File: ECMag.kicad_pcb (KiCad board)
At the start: 2 copper layers, 44 parts, among them J1 Conn_01x12, J2 Conn_01x05, J3 Conn_01x04, J4 USB_B, J5 Barrel_Jack_SW, J6 Conn_01x04, K1 Tactil Switch B3F NA, K2 Tactil Switch B3F NA, K3 Tactil Switch B3F NA, K4 Tactil Switch B3F NA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

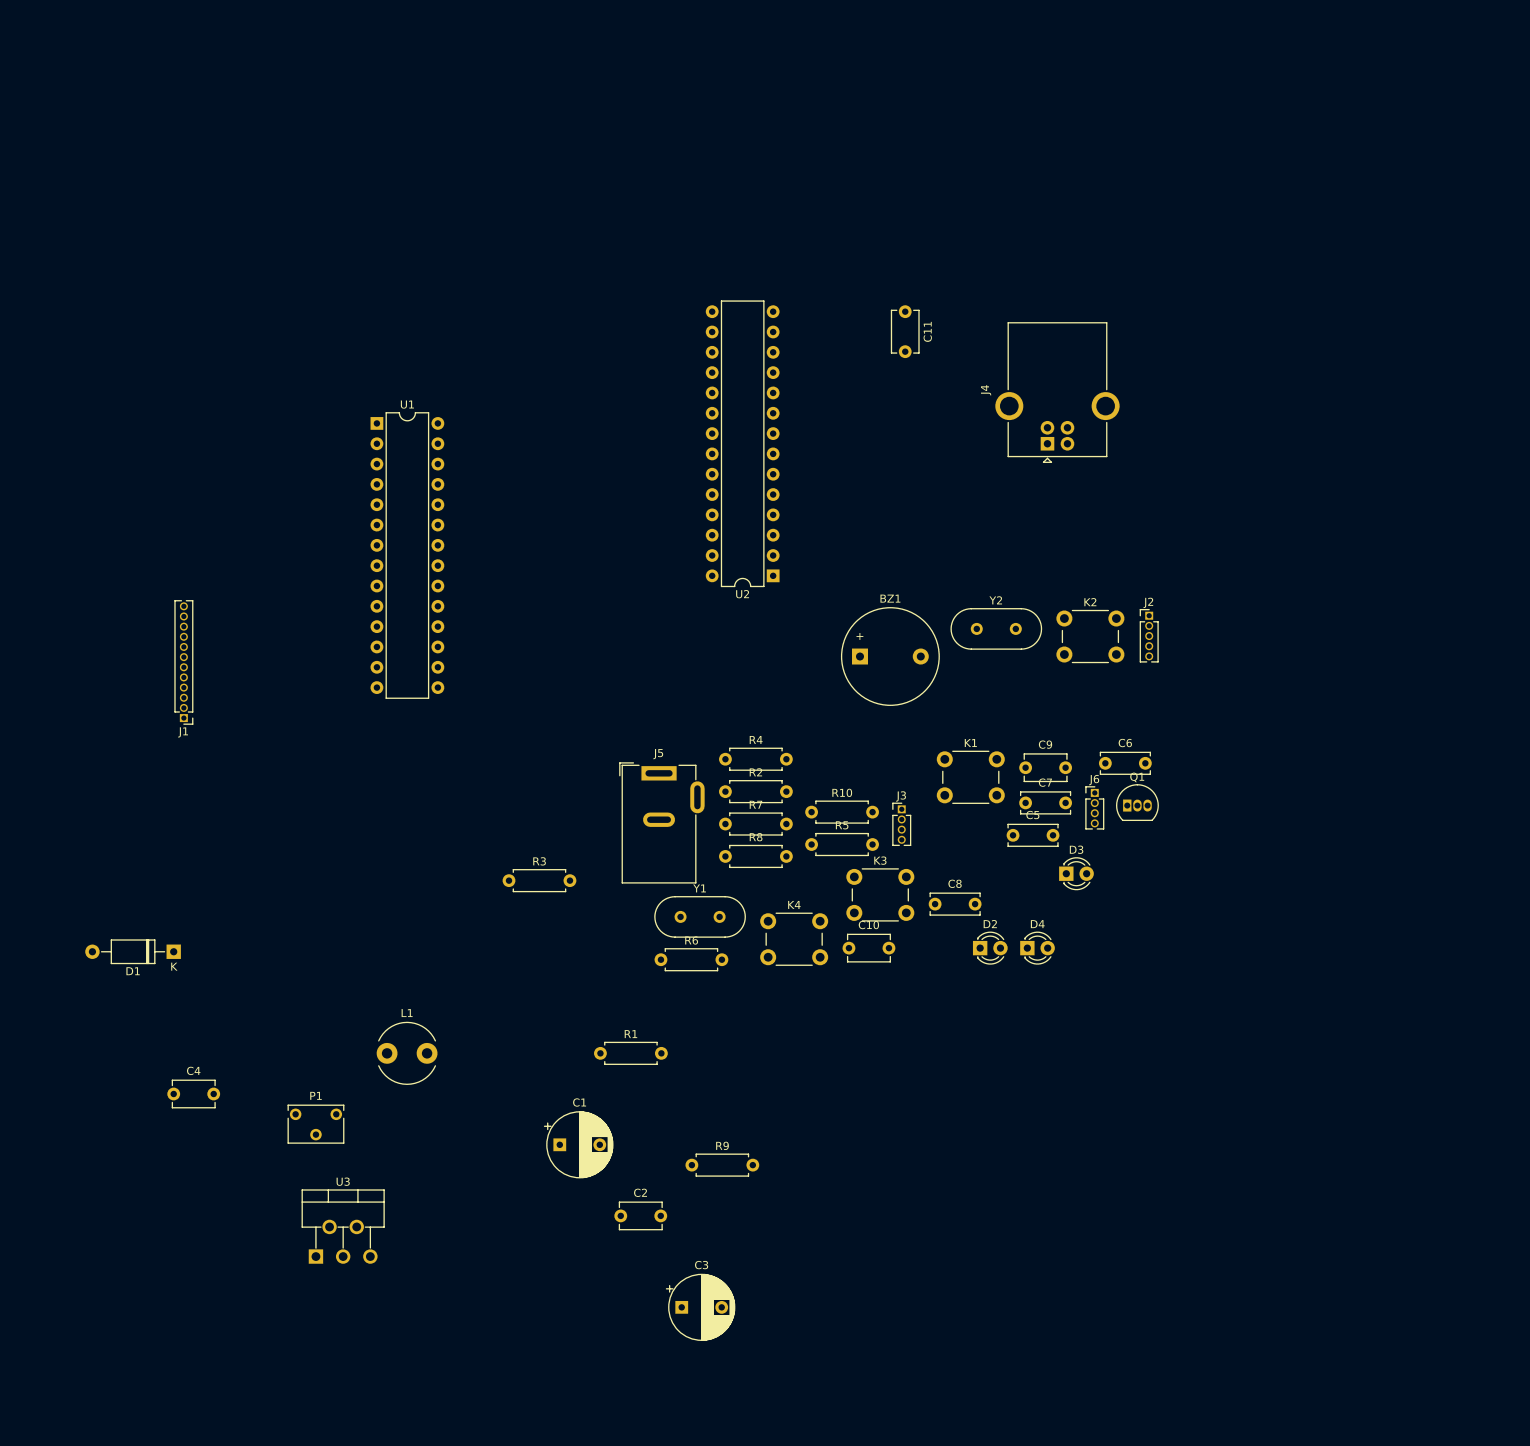
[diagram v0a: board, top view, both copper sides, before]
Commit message: agregado de valores de los componentes en el esquemático
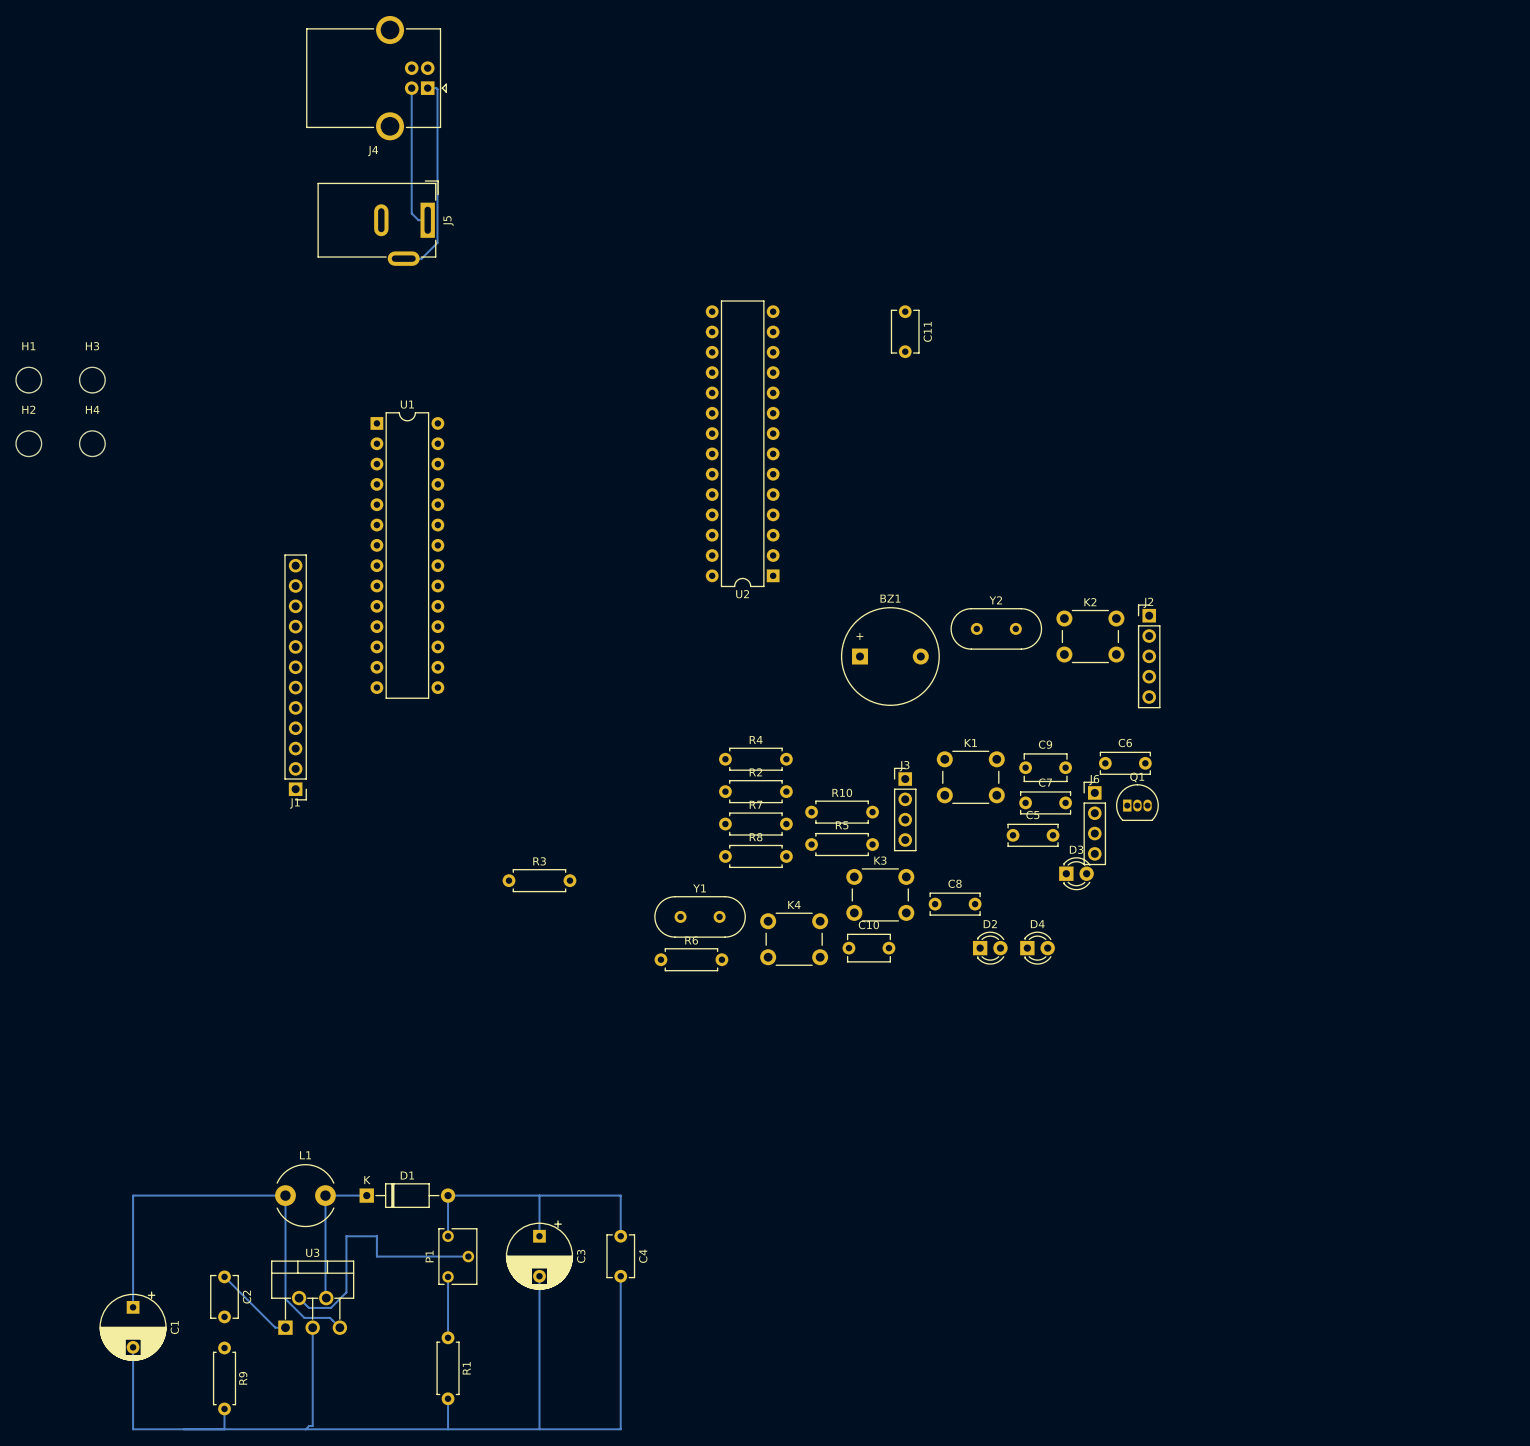
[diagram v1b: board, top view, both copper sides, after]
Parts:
- added H1: MountingHole, MountingHole:MountingHole_3.2mm_M3, F.Cu at (34.0, 61.9)
- added H2: MountingHole, MountingHole:MountingHole_3.2mm_M3, F.Cu at (34.0, 69.8)
- added H3: MountingHole, MountingHole:MountingHole_3.2mm_M3, F.Cu at (41.9, 61.9)
- added H4: MountingHole, MountingHole:MountingHole_3.2mm_M3, F.Cu at (41.9, 69.8)
- BZ1: value Buzzer 5V 85db 2300Hz -> 85db 2300Hz
- C1, C3: value 220uF 25v HT -> 220uF 25v
- C2: value 330nF Cerámico -> 330nF
- C4: value 100nF Cerámico -> 100nF
- D2: value LED Azul -> LED A
- D3: value LED Rojo -> LED R
- D4: value LED Verde -> LED V
- J1: footprint Connector_PinHeader_1.27mm:PinHeader_1x12_P1.27mm_Vertical -> Connector_PinHeader_2.54mm:PinHeader_1x12_P2.54mm_Vertical
- J2: footprint Connector_PinHeader_1.27mm:PinHeader_1x05_P1.27mm_Vertical -> Connector_PinHeader_2.54mm:PinHeader_1x05_P2.54mm_Vertical
- J3, J6: footprint Connector_PinHeader_1.27mm:PinHeader_1x04_P1.27mm_Vertical -> Connector_PinHeader_2.54mm:PinHeader_1x04_P2.54mm_Vertical
- R1: value 2K 1% -> 2K
- R10: value 3K3 5% -> 3K3
- R2, R3, R4, R5: value 10K 5% -> 10K
- R6, R7, R8: value 4K7 5% -> 4K7
- R9: value 2K2 1% -> 2K2
- moved J4 89.3 mm to (83.8, 25.4), turned to 180 degrees
- moved J5 74.9 mm to (83.8, 41.9), turned to 270 degrees
- moved R9 62.7 mm to (58.4, 182.9), turned to 270 degrees
- moved C4 58.6 mm to (108.0, 168.9), turned to 270 degrees
- moved C1 57.1 mm to (47.0, 177.8), turned to 270 degrees
- moved C2 50.1 mm to (58.4, 174.0), turned to 270 degrees
- moved R1 40.3 mm to (86.4, 181.6), turned to 270 degrees
- moved D1 38.9 mm to (76.2, 163.8), turned to 0 degrees
- moved L1 21.8 mm to (66.0, 163.8)
- moved P1 20.7 mm to (86.4, 168.9), turned to 90 degrees
- moved C3 19.9 mm to (97.8, 168.9), turned to 270 degrees
- moved J1 16.6 mm to (67.3, 113.0)
- moved U3 9.67 mm to (66.0, 180.3)
- moved J3 3.81 mm to (143.5, 111.8)
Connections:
- Y1 pad 1: Net-(C5-Pad1) -> Net-(C6-Pad1)
- Y1 pad 2: Net-(C6-Pad1) -> Net-(C5-Pad1)
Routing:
- net GND: track 0.00 -> 152.2 mm
- net +5V: track 0.00 -> 54.2 mm
- net +12V: track 0.00 -> 36.8 mm
- net Net-(P1-Pad2): track 0.00 -> 32.0 mm
- net Net-(J4-Pad1): track 0.00 -> 25.5 mm
- net Net-(D1-Pad1): track 0.00 -> 18.0 mm
- net Net-(C2-Pad1): track 0.00 -> 10.3 mm
- net Net-(P1-Pad3): track 0.00 -> 7.62 mm

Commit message: Edicion de huella de pulsadores y primer pcb
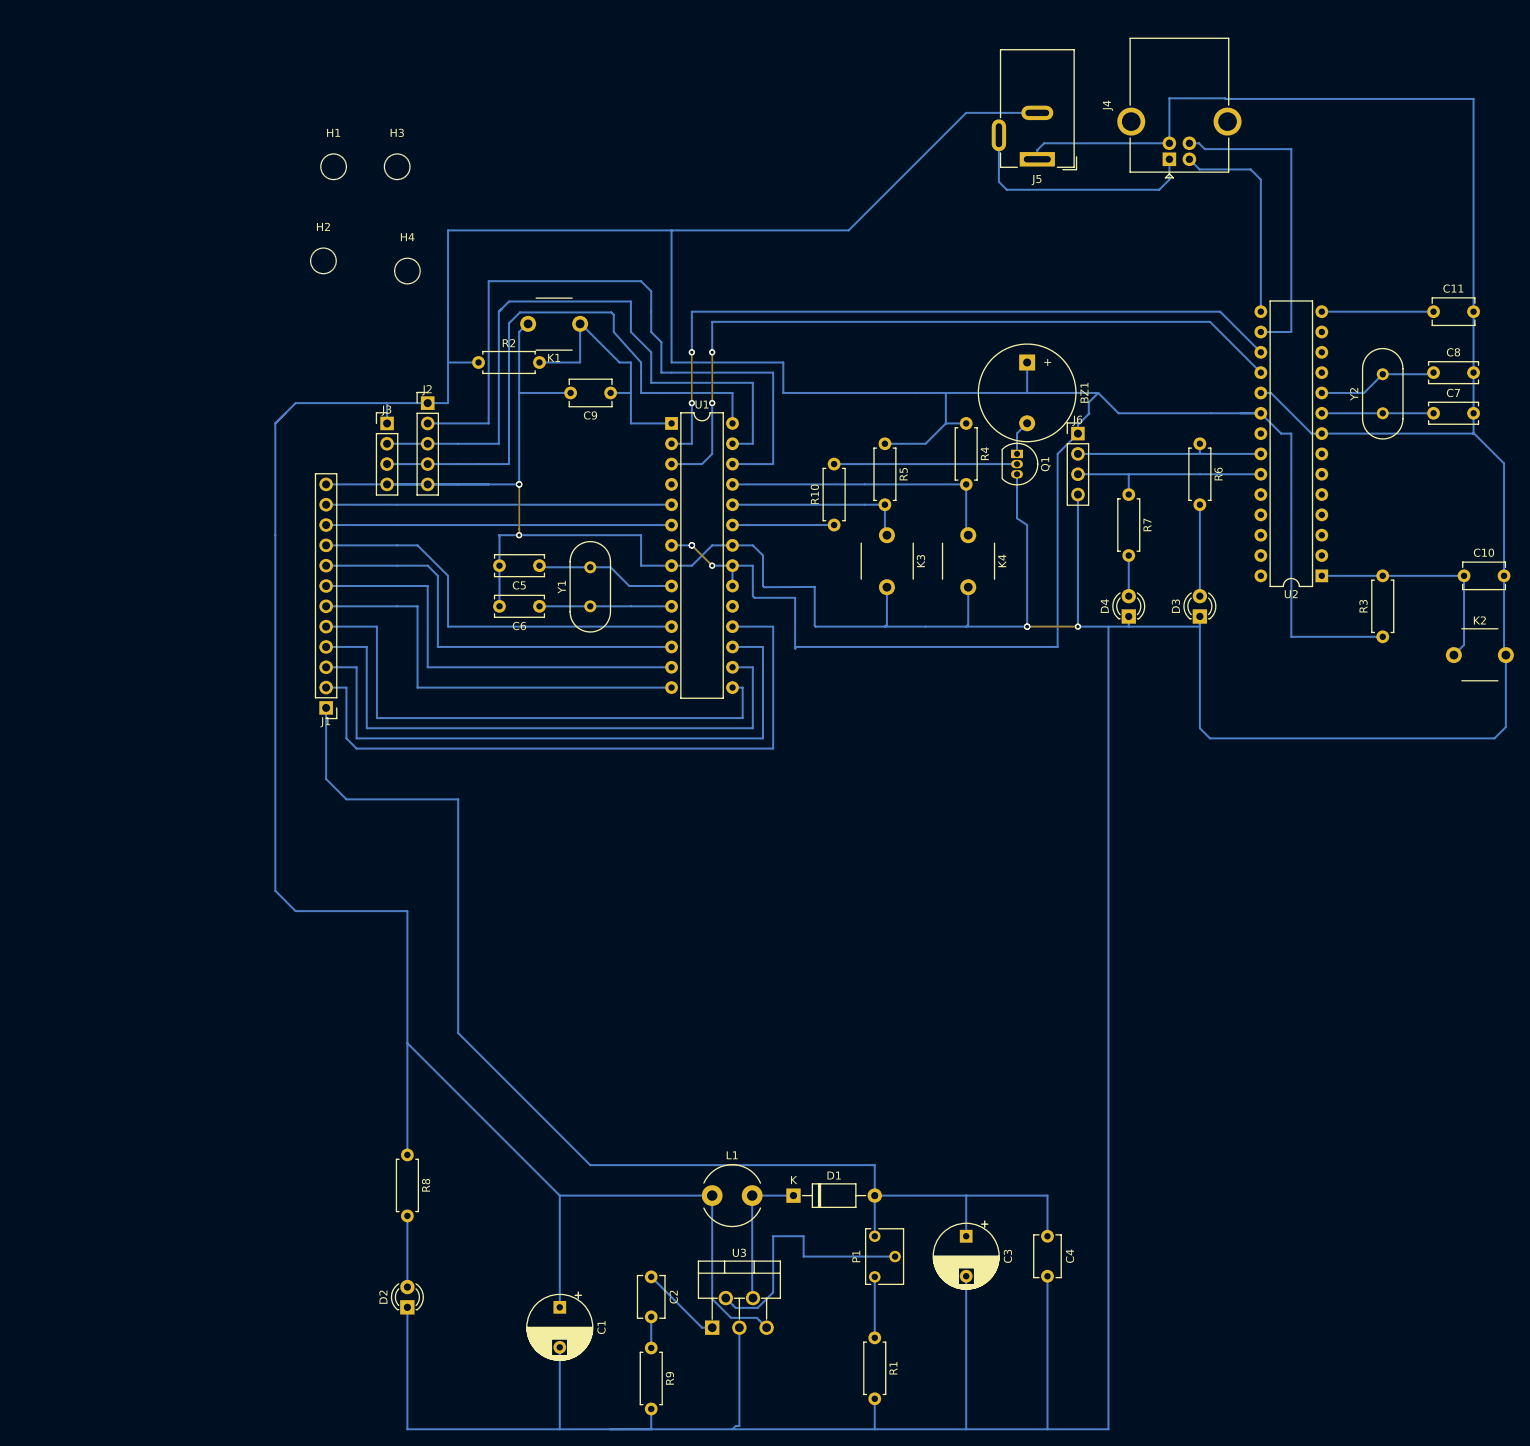
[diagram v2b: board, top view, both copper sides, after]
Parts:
- K1, K3, K4: value Tactil Switch B3F NA -> Tactil Switch NA; footprint Button_Switch_THT:SW_PUSH_6mm_H5mm -> EMS_huellas:SW_6x5mm_2C
- K2: footprint Button_Switch_THT:SW_PUSH_6mm_H5mm -> EMS_huellas:SW_6x5mm_2C
- moved R3 113.4 mm to (203.2, 94.0), turned to 90 degrees
- moved J2 94.0 mm to (83.8, 64.8)
- moved R6 93.3 mm to (180.3, 69.8), turned to 270 degrees
- moved J4 93.1 mm to (176.5, 34.3), turned to 90 degrees
- moved C8 91.1 mm to (209.6, 61.0)
- moved C10 89.9 mm to (213.4, 86.4)
- moved D2 84.5 mm to (81.3, 177.8), turned to 90 degrees
- moved J3 78.6 mm to (78.7, 67.3)
- moved J5 76.6 mm to (160.0, 34.3), turned to 180 degrees
- moved C6 73.4 mm to (97.8, 90.2), turned to 180 degrees
- moved C7 70.5 mm to (209.6, 66.0)
- moved C9 69.9 mm to (106.7, 63.5), turned to 180 degrees
- moved K1 69.3 mm to (102.9, 57.1), turned to 180 degrees
- moved U2 68.6 mm to (195.6, 86.4)
- moved C5 68.1 mm to (97.8, 85.1), turned to 180 degrees
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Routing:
- net GND: track 152.2 -> 729.1 mm, vias 0 -> 6
- net +5V: track 54.2 -> 574.0 mm, vias 0 -> 3
- net +12V: track 36.8 -> 155.2 mm
- net /TxRx: track 0.00 -> 93.3 mm, vias 0 -> 2
- net /RxTx: track 0.00 -> 92.3 mm, vias 0 -> 2
- net /DRDY: track 0.00 -> 87.4 mm
- net /a1: track 0.00 -> 83.1 mm
- net /SDA: track 0.00 -> 82.1 mm
- net /a2: track 0.00 -> 78.7 mm
- net /a3: track 0.00 -> 73.7 mm
- net /SCL: track 0.00 -> 72.9 mm
- net /a4: track 0.00 -> 68.6 mm
- net /a6: track 0.00 -> 53.3 mm
- net /a5: track 0.00 -> 53.3 mm
- net /a7: track 0.00 -> 52.6 mm
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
